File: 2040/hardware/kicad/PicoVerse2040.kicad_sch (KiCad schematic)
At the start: 23 parts, among them J1 MSX_Slot, Q1 BSS138, Q2 BSS138, Q3 BSS138, Q4 BSS138, Q5 BSS138, U1 WeAct-RP2040-Pico

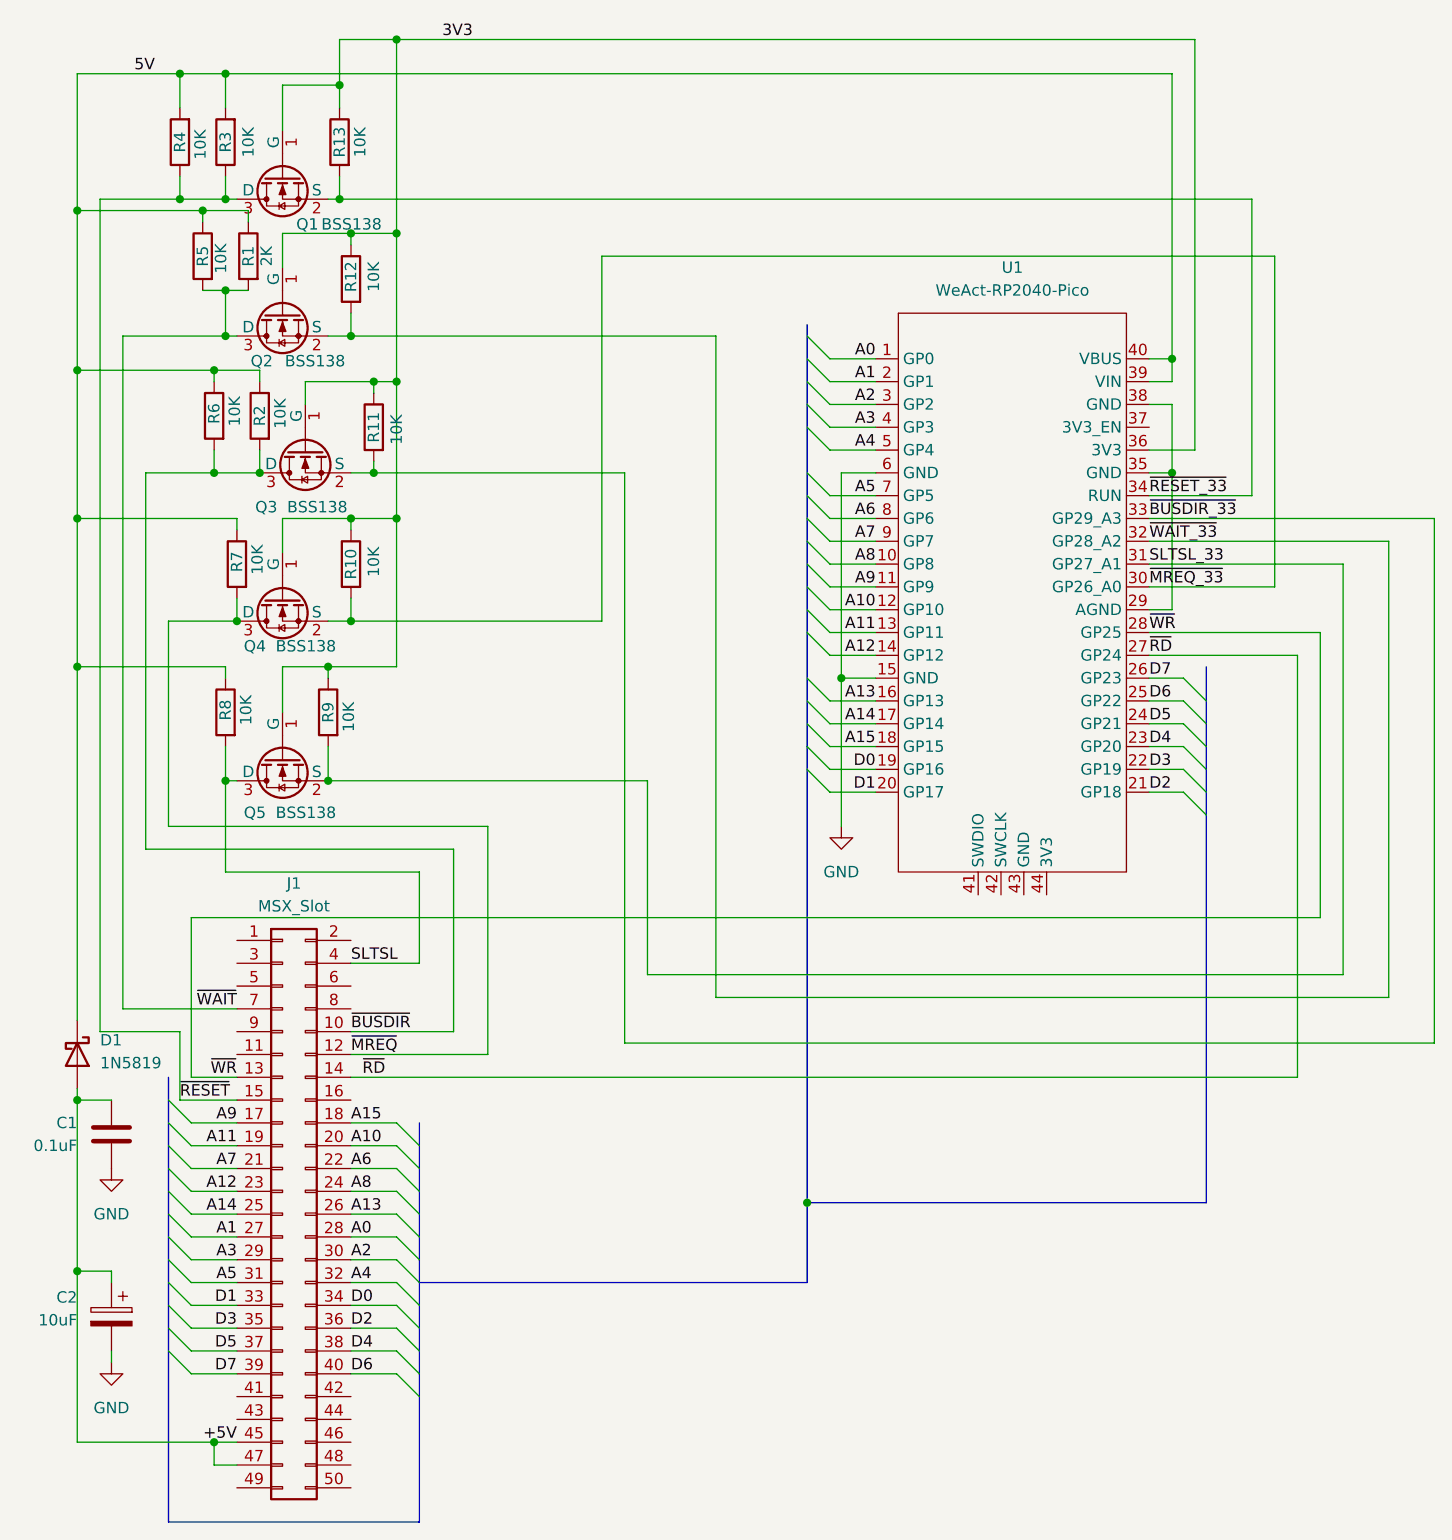
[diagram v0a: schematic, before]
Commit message: Fix MREQ <-> IORQ
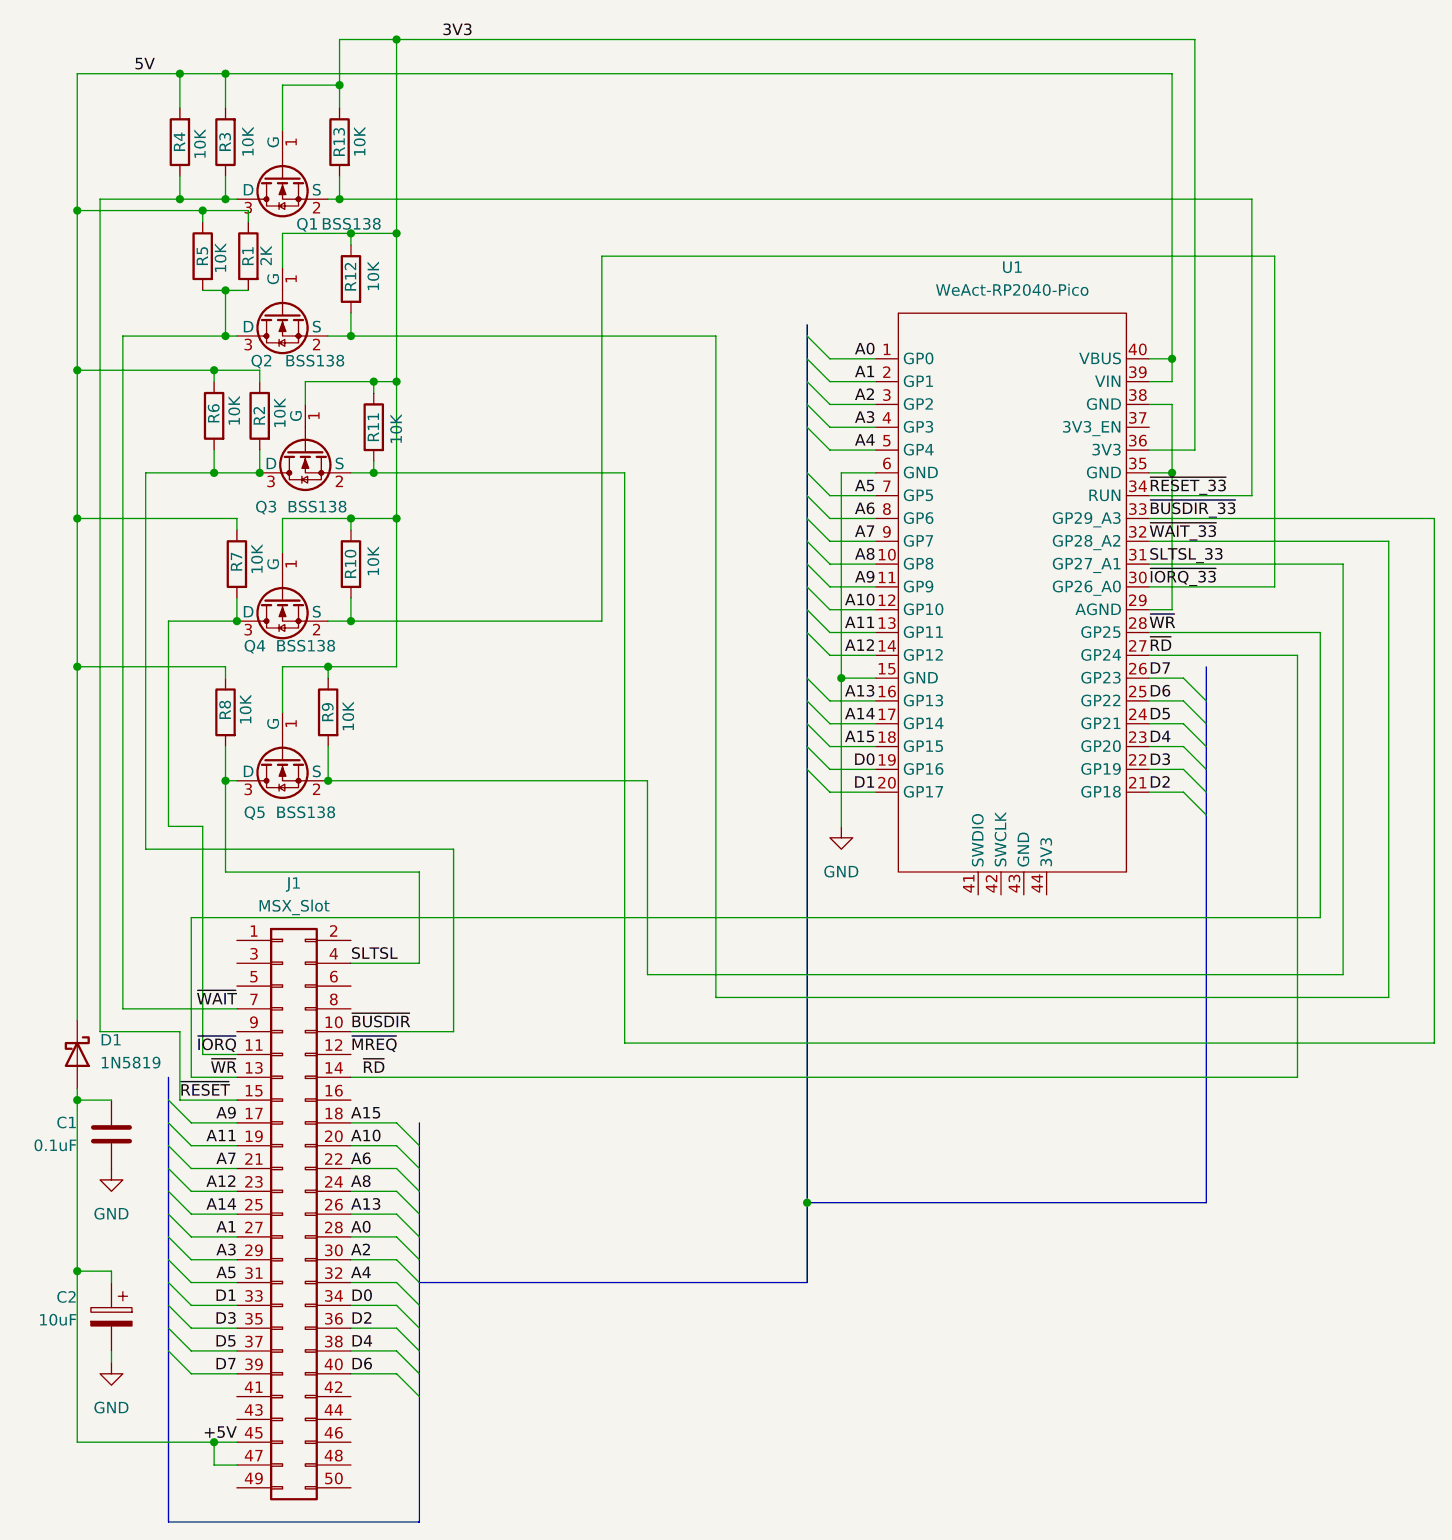
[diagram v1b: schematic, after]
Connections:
- net ~{MREQ}: no longer Q4.3 (D), R7.2
- net ~{IORQ}: now reaches J1.11 (Pin_11)
- net ~{IORQ}: now also Q4.3 (D), R7.2
- net ~{MREQ_33} renamed ~{IORQ_33}
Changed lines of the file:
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@@
+	(wire
+		(pts
+			(xy 87.63 140.97) (xy 83.82 140.97)
+		)
+		(stroke
+			(width 0)
+			(type default)
+		)
+	)
 	(wire
 		(pts
@@
 	(wire
 		(pts
+			(xy 83.82 140.97) (xy 83.82 115.57)
+		)
+		(stroke
+			(width 0)
+			(type default)
+		)
+	)
+	(wire
+		(pts
 			(xy 105.41 49.53) (xy 105.41 27.94)
 		)
@@
 	(wire
 		(pts
-			(xy 100.33 140.97) (xy 115.57 140.97)
-		)
-		(stroke
-			(width 0)
-			(type default)
-		)
-	)
-	(wire
-		(pts
 			(xy 200.66 45.72) (xy 200.66 78.74)
 		)
@@
 	(wire
 		(pts
-			(xy 80.01 115.57) (xy 115.57 115.57)
+			(xy 80.01 115.57) (xy 83.82 115.57)
 		)
 		(stroke
@@
 		(pts
 			(xy 189.23 99.06) (xy 193.04 99.06)
-		)
-		(stroke
-			(width 0)
-			(type default)
-		)
-	)
-	(wire
-		(pts
-			(xy 115.57 140.97) (xy 115.57 115.57)
 		)
 		(stroke
@@
 		)
 	)
-	(label "~{MREQ_33}"
+	(label "~{IORQ_33}"
 		(at 189.23 88.9 0)
 		(effects
@@
 		)
 	)
+	(label "~{IORQ}"
+		(at 87.63 140.97 180)
+		(effects
+			(font
+				(size 1.27 1.27)
+			)
+			(justify right bottom)
+		)
+	)

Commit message: Fix bugs
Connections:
- net 5V: now also R1.2, R2.2, R5.2, R6.2, R7.2, R8.2; no longer R1.1, R2.1, R5.1, R6.1, R7.1, R8.1
- net SLTSL: now also R8.1; no longer R8.2
- net ~{BUSDIR}: now also R2.1, R6.1; no longer R2.2, R6.2
- net ~{IORQ}: now also R7.1; no longer R7.2
- net ~{WAIT}: now also R1.1, R5.1; no longer R1.2, R5.2
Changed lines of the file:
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@@
 	)
 	(symbol
+		(lib_name "R_6")
 		(lib_id "Device:R")
-		(at 88.9 52.07 0)
-		(mirror y)
+		(at 88.9 52.07 180)
 		(unit 1)
 		(body_style 1)
@@
 	)
 	(symbol
+		(lib_name "R_5")
 		(lib_id "Device:R")
-		(at 90.17 69.85 0)
-		(mirror y)
+		(at 90.17 69.85 180)
 		(unit 1)
 		(body_style 1)
@@
 		)
 		(property "Value" "10K"
-			(at 92.456 69.596 90)
+			(at 92.456 70.104 90)
 			(show_name no)
 			(do_not_autoplace no)
@@
 	)
 	(symbol
+		(lib_name "R_3")
 		(lib_id "Device:R")
-		(at 83.82 52.07 0)
-		(mirror y)
+		(at 83.82 52.07 180)
 		(unit 1)
 		(body_style 1)
@@
 		)
 		(property "Value" "10K"
-			(at 85.852 52.324 90)
+			(at 85.852 51.816 90)
 			(show_name no)
 			(do_not_autoplace no)
@@
 	)
 	(symbol
+		(lib_name "R_7")
 		(lib_id "Device:R")
 		(at 86.36 39.37 180)
@@
 	)
 	(symbol
+		(lib_name "R_4")
 		(lib_id "Device:R")
-		(at 85.09 69.85 0)
-		(mirror y)
+		(at 85.09 69.85 180)
 		(unit 1)
 		(body_style 1)
@@
 		(dnp no)
 		(property "Reference" "R6"
-			(at 85.09 69.596 90)
+			(at 85.09 70.104 90)
 			(show_name no)
 			(do_not_autoplace no)
@@
 		)
 		(property "Value" "10K"
-			(at 87.376 69.342 90)
+			(at 87.376 70.358 90)
 			(show_name no)
 			(do_not_autoplace no)
@@
 	)
 	(symbol
+		(lib_name "R_1")
 		(lib_id "Device:R")
-		(at 87.63 86.36 0)
-		(mirror y)
+		(at 87.63 86.36 180)
 		(unit 1)
 		(body_style 1)
@@
 		(dnp no)
 		(property "Reference" "R7"
-			(at 87.63 86.106 90)
+			(at 87.63 86.614 90)
 			(show_name no)
 			(do_not_autoplace no)
@@
 		)
 		(property "Value" "10K"
-			(at 89.916 85.852 90)
+			(at 89.916 86.868 90)
 			(show_name no)
 			(do_not_autoplace no)
@@
 	)
 	(symbol
+		(lib_name "R_8")
 		(lib_id "Device:R")
 		(at 81.28 39.37 180)
@@
 	)
 	(symbol
+		(lib_name "R_2")
 		(lib_id "Device:R")
-		(at 86.36 102.87 0)
-		(mirror y)
+		(at 86.36 102.87 180)
 		(unit 1)
 		(body_style 1)
@@
 		(dnp no)
 		(property "Reference" "R8"
-			(at 86.36 102.616 90)
+			(at 86.36 103.124 90)
 			(show_name no)
 			(do_not_autoplace no)
@@
 		)
 		(property "Value" "10K"
-			(at 88.646 102.616 90)
-			(show_name no)
-			(do_not_autoplace no)
+			(at 88.646 103.124 90)
+			(show_name no)
+			(do_not_autoplace no)

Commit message: Fix pcb
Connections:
- net +5V: now also C1.2; no longer C1.1
- net GND: now also C1.1; no longer C1.2
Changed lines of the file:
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@@
 	(symbol
 		(lib_id "Device:C")
-		(at 73.66 149.86 0)
-		(mirror y)
+		(at 73.66 149.86 180)
 		(unit 1)
 		(body_style 1)
@@
 		(dnp no)
 		(property "Reference" "C1"
-			(at 69.85 148.5899 0)
+			(at 69.85 151.1301 0)
 			(show_name no)
 			(do_not_autoplace no)
@@
 		)
 		(property "Value" "0.1uF"
-			(at 69.85 151.1299 0)
+			(at 69.85 148.5901 0)
 			(show_name no)
 			(do_not_autoplace no)
@@
 		)
 		(property "Footprint" "Capacitor_SMD:C_0603_1608Metric_Pad1.08x0.95mm_HandSolder"
-			(at 72.6948 153.67 0)
+			(at 72.6948 146.05 0)
 			(hide yes)
 			(show_name no)
